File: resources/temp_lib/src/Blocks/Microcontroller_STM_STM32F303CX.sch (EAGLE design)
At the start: 8 parts, among them SW1 B3U

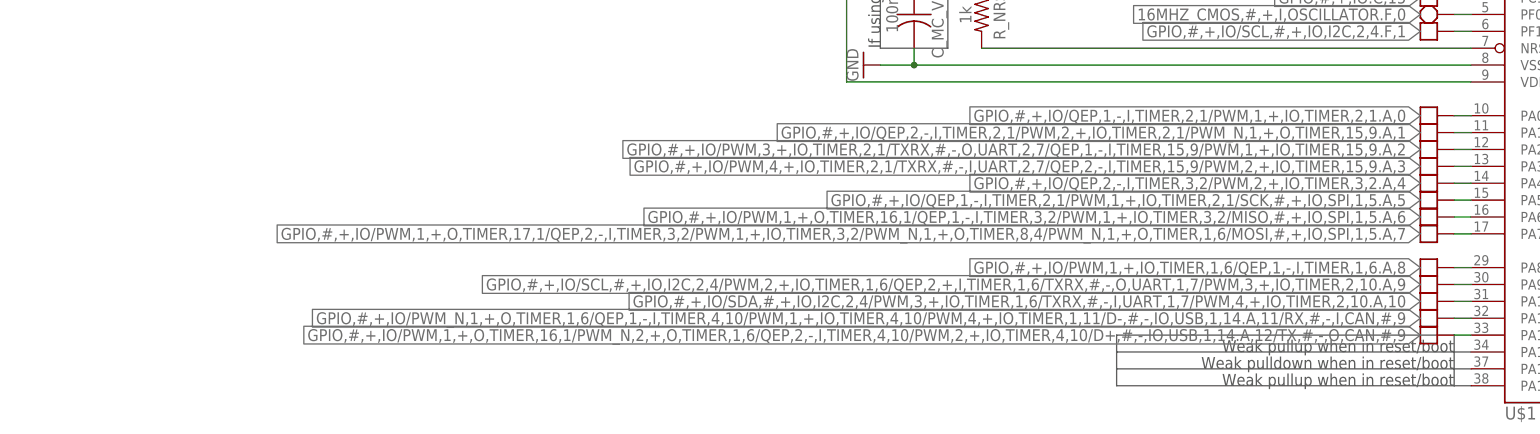
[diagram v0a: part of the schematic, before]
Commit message: Moved all electronics library schematics to temporary location.
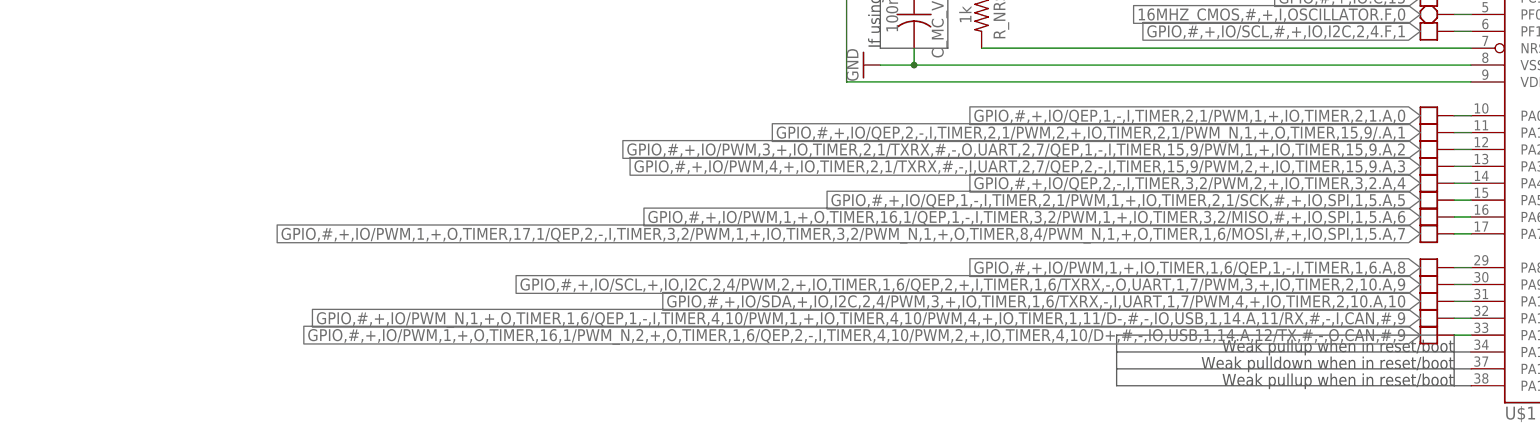
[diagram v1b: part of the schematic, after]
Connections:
- net GPIO,#,+,IO/QEP,2,-,I,TIMER,2,1/PWM,2,+,IO,TIMER,2,1/PWM_N,1,+,O,TIMER,15,9.A,1 renamed GPIO,#,+,IO/QEP,2,-,I,TIMER,2,1/PWM,2,+,IO,TIMER,2,1/PWM_N,1,+,O,TIMER,15,9/.A,1
- net GPIO,#,+,IO/SCL,#,+,IO,I2C,2,4/PWM,2,+,IO,TIMER,1,6/QEP,2,+,I,TIMER,1,6/TXRX,#,-,O,UART,1,7/PWM,3,+,IO,TIMER,2,10.A,9 renamed GPIO,#,+,IO/SCL,+,IO,I2C,2,4/PWM,2,+,IO,TIMER,1,6/QEP,2,+,I,TIMER,1,6/TXRX,-,O,UART,1,7/PWM,3,+,IO,TIMER,2,10.A,9
- net GPIO,#,+,IO/SDA,#,+,IO,I2C,2,4/PWM,3,+,IO,TIMER,1,6/TXRX,#,-,I,UART,1,7/PWM,4,+,IO,TIMER,2,10.A,10 renamed GPIO,#,+,IO/SDA,+,IO,I2C,2,4/PWM,3,+,IO,TIMER,1,6/TXRX,-,I,UART,1,7/PWM,4,+,IO,TIMER,2,10.A,10
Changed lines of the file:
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@@
 </segment>
 </net>
-<net name="GPIO,#,+,IO/QEP,2,-,I,TIMER,2,1/PWM,2,+,IO,TIMER,2,1/PWM_N,1,+,O,TIMER,15,9.A,1" class="0">
+<net name="GPIO,#,+,IO/QEP,2,-,I,TIMER,2,1/PWM,2,+,IO,TIMER,2,1/PWM_N,1,+,O,TIMER,15,9/.A,1" class="0">
 <segment>
 <pinref part="U$1" gate="G$1" pin="PA1"/>
@@
 </segment>
 </net>
-<net name="GPIO,#,+,IO/SCL,#,+,IO,I2C,2,4/PWM,2,+,IO,TIMER,1,6/QEP,2,+,I,TIMER,1,6/TXRX,#,-,O,UART,1,7/PWM,3,+,IO,TIMER,2,10.A,9" class="0">
+<net name="GPIO,#,+,IO/SCL,+,IO,I2C,2,4/PWM,2,+,IO,TIMER,1,6/QEP,2,+,I,TIMER,1,6/TXRX,-,O,UART,1,7/PWM,3,+,IO,TIMER,2,10.A,9" class="0">
 <segment>
 <pinref part="U$1" gate="G$1" pin="PA9"/>
@@
 </segment>
 </net>
-<net name="GPIO,#,+,IO/SDA,#,+,IO,I2C,2,4/PWM,3,+,IO,TIMER,1,6/TXRX,#,-,I,UART,1,7/PWM,4,+,IO,TIMER,2,10.A,10" class="0">
+<net name="GPIO,#,+,IO/SDA,+,IO,I2C,2,4/PWM,3,+,IO,TIMER,1,6/TXRX,-,I,UART,1,7/PWM,4,+,IO,TIMER,2,10.A,10" class="0">
 <segment>
 <pinref part="U$1" gate="G$1" pin="PA10"/>
